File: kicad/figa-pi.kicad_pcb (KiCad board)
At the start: 4 copper layers, 65 x 56 mm, 147 parts, among them J1 BH-10(IDC-10MS), J2 PLS-2, J3 PBD-40(DS1023-2x20), J4 PLD-10(DS1021-2x5), J5 L829-1J1T-43, J6 POE connector, J7 PLS-1, J8 PLS-1, J9 PLS-1, U1 CAT24C32WI, U10 TLV62084DSGR, U11 TLV62084DSGR, U2 ASEMB-25.000MHZ-LC-T, U3 NUP4114UPXV6T1G, U5 10CL025ZE144, U6 KSZ9021GN, U7 CDCLVC1102PW, U9 TLV62084DSGR

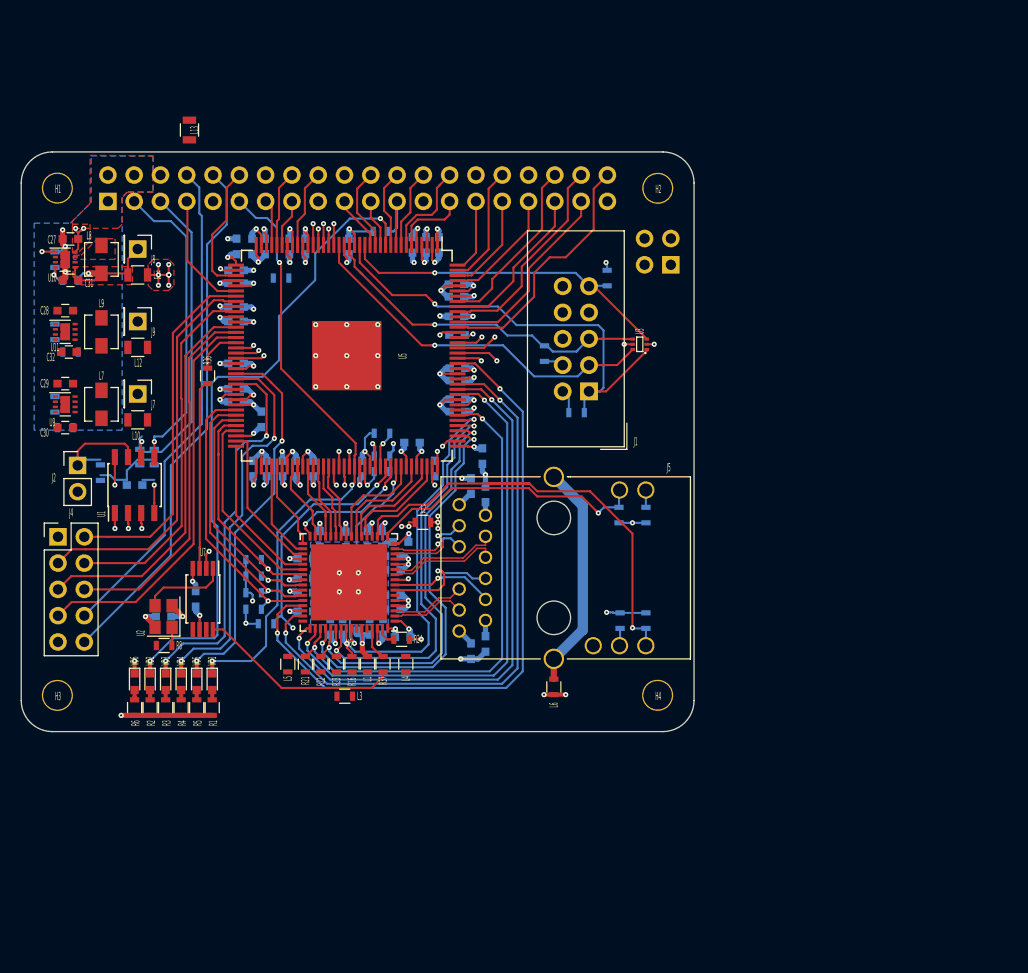
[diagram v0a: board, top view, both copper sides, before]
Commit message: Added LOGO as footprint Added fields for all components Renamed BOM file. Updated BOM file. Updated project fields.
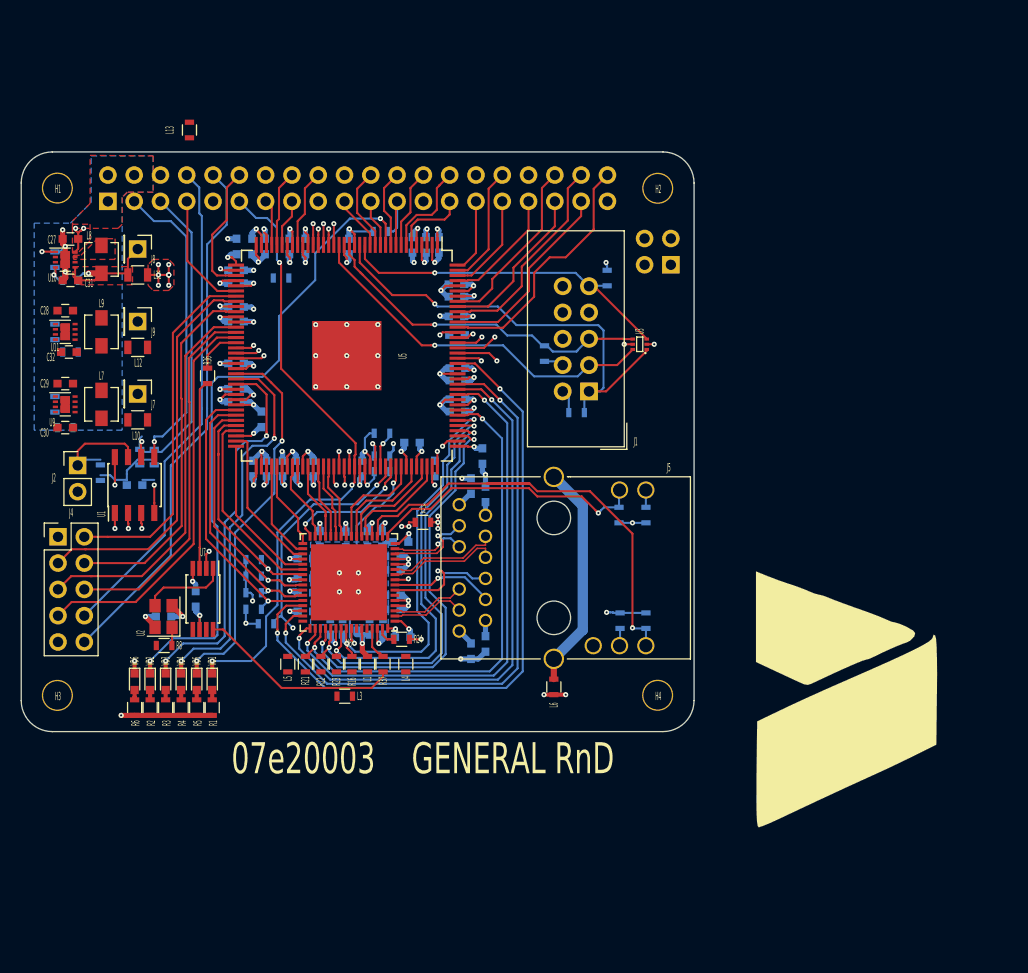
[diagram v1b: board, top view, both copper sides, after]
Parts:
- added G***: LOGO, library:LogoGenRND_18x25mm, F.Cu at (158.3, 113.7)
- C1, C10, C11, C12, C13, C18, C19, C2, C20, C21, C25, C3, C35, C36, C38, C39, C4, C41, C42, C43, C44, C45, C46, C47, C48, C5, C54, C56, C58, C60, C61, C63, C65, C66, C7, C8, C9: value 0.1u -> 0.1uF
- C14, C15, C16, C17: value 0.1u 16V -> 0.1uF
- C22, C23, C24, C26, C33, C34, C37, C40, C6, C62, C64: value 10u -> 10uF
- C27, C28, C29: value 10u 16V -> 10uF
- C30, C31, C32: value 22u 6v3 -> 22uF
- C49, C50, C51, C52, C53, C55, C57, C59: value 0.01u -> 0.01uF
- L13: footprint Inductors_SMD:L_0805 -> Inductors_SMD:L_0603
- R11, R12: value 3.9k -> 3.92k
- R30: value 178k 1% -> 127k 1%
- R31, R35: value 39.2k 1% -> 28k 1%
- R34: value 65.3k 1% -> 46.4k 1%
- U1: value CAT24C32WI -> 24LC32A/SN
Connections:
- net IO_85 renamed IO_31
- net IO_86 renamed IO_32
- net IO_87 renamed IO_28
- net IO_99 renamed IO_33
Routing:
- net (no net): track 0.00 -> 7.87 mm
- net +3V3: track 70.8 -> 64.1 mm
- net GND: track 221.8 -> 220.6 mm
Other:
- board text added: "07e20003"
- board text added: "GENERAL RnD"

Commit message: Removed footprint for unused components Updated 3d model for LQFP-144 Updated symbol library Updated schematics Updated PCB - finished routing
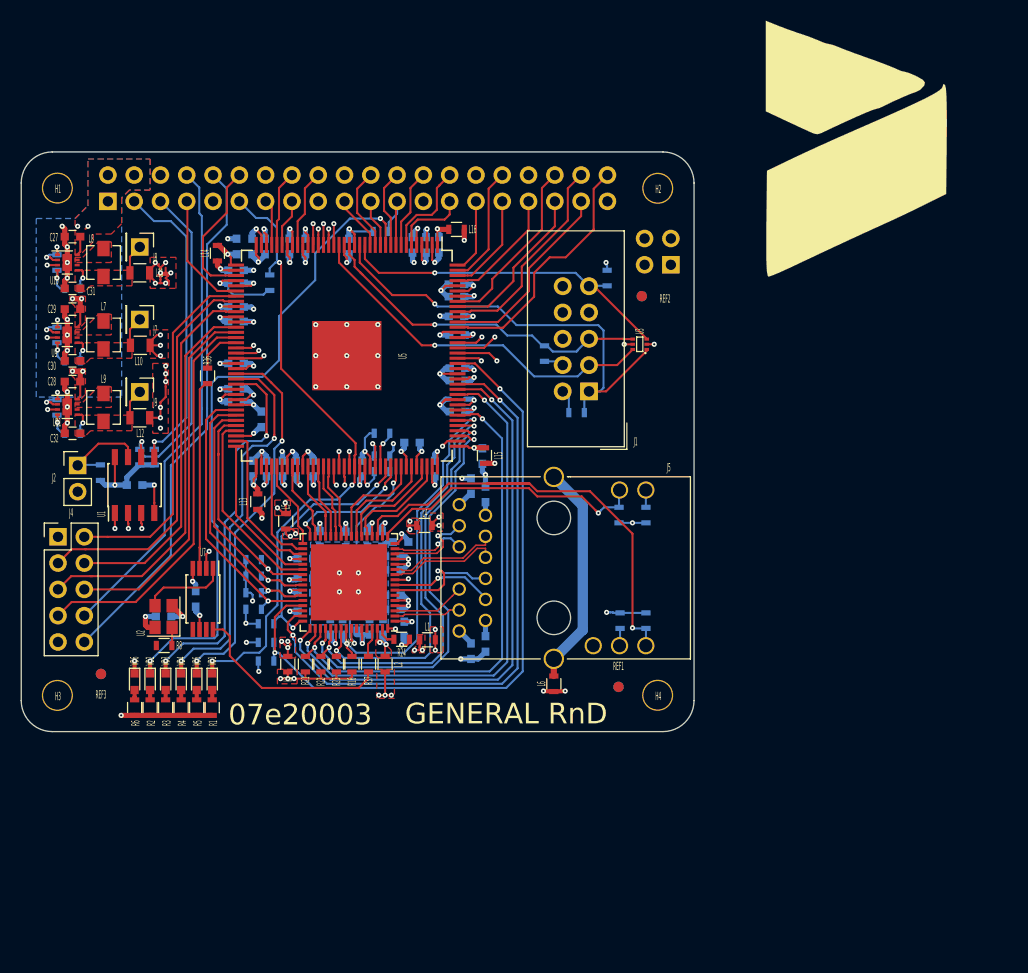
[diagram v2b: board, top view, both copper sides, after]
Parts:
- removed C51: 0.01uF, Capacitors_SMD:C_0603
- added L14: BLM18PG330SN1D, Inductors_SMD:L_0603, F.Cu at (97.5, 70.6)
- added L15: BLM18PG330SN1D, Inductors_SMD:L_0603, F.Cu at (123.3, 90.2)
- added L16: BLM18PG330SN1D, Inductors_SMD:L_0603, F.Cu at (120.6, 68.3)
- added R41: DNI_4.99k 1%, Resistors_SMD:R_0603, B.Cu at (102.2, 108.2)
- added R42: 1k, Resistors_SMD:R_0603, B.Cu at (102.2, 110.0)
- added REF1: Fiducial_1mm_Dia_2.54mm_Outer_CopperTop, Fiducials:Fiducial_1mm_Dia_2.54mm_Outer_CopperTop, F.Cu at (136.2, 112.5)
- added REF2: Fiducial_1mm_Dia_2.54mm_Outer_CopperTop, Fiducials:Fiducial_1mm_Dia_2.54mm_Outer_CopperTop, F.Cu at (138.5, 74.8)
- added REF3: Fiducial_1mm_Dia_2.54mm_Outer_CopperTop, Fiducials:Fiducial_1mm_Dia_2.54mm_Outer_CopperTop, B.Cu at (86.2, 111.2)
- added REF3: Fiducial_1mm_Dia_2.54mm_Outer_CopperTop, Fiducials:Fiducial_1mm_Dia_2.54mm_Outer_CopperTop, F.Cu at (86.2, 111.2)
- added REF4: Fiducial_1mm_Dia_2.54mm_Outer_CopperTop, Fiducials:Fiducial_1mm_Dia_2.54mm_Outer_CopperTop, B.Cu at (138.5, 74.8)
- added REF5: Fiducial_1mm_Dia_2.54mm_Outer_CopperTop, Fiducials:Fiducial_1mm_Dia_2.54mm_Outer_CopperTop, B.Cu at (136.2, 112.5)
- moved G*** 53.2 mm to (159.2, 60.5)
- moved L13 36.5 mm to (101.4, 94.6)
- moved C37 31.2 mm to (99.3, 70.0), turned to 90 degrees
- moved C49 28.1 mm to (101.0, 91.4), turned to 90 degrees
- moved C41 22.2 mm to (123.1, 90.2), turned to 270 degrees
- moved C45 19.6 mm to (118.9, 69.8), turned to 270 degrees
- moved L2 14.2 mm to (113.7, 110.3), turned to 270 degrees
- moved L5 13.8 mm to (104.1, 96.5), turned to 90 degrees
- moved L4 13.5 mm to (117.5, 96.9), turned to 0 degrees
- moved C32 7.86 mm to (83.5, 88.0)
- moved R34 7.85 mm to (83.5, 88.0)
- moved L9 7.30 mm to (86.5, 85.5)
- moved R35 7.30 mm to (82.0, 85.5)
- moved U11 7.25 mm to (83.0, 85.5)
- moved C29 7.23 mm to (83.5, 76.0)
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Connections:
- net 25M_A renamed /interface.sch/FPGA_25M
- net 25M_B renamed /ethernet.sch/PHY_25M
- net CLK_125M renamed /ethernet.sch/CLK_125M
- net DATA renamed /interface.sch/DATA
- net DCLK renamed /interface.sch/DCLK
- net GTX_CLK renamed /ethernet.sch/GTX_CLK
- net INT_N renamed /ethernet.sch/INT_N
- net IO_10 renamed /interface.sch/IO_10
- net IO_133 renamed /interface.sch/IO_133
- net IO_141 renamed /interface.sch/IO_141
- net IO_142 renamed /interface.sch/IO_142
- net IO_143 renamed /interface.sch/IO_143
- net IO_144 renamed /interface.sch/IO_144
- net IO_28 renamed /interface.sch/IO_28
- net IO_31 renamed /interface.sch/IO_31
- net IO_32 renamed /interface.sch/IO_32
- net IO_33 renamed /interface.sch/IO_33
- net IO_39 renamed /interface.sch/IO_39
- net IO_42 renamed /interface.sch/IO_42
- net IO_6 renamed /interface.sch/IO_6
- net IO_7 renamed /interface.sch/IO_7
- net IO_8 renamed /interface.sch/IO_8
- net JTAG_TCK renamed /interface.sch/JTAG_TCK
- net JTAG_TDI renamed /interface.sch/JTAG_TDI
- net JTAG_TDO renamed /interface.sch/JTAG_TDO
- net JTAG_TMS renamed /interface.sch/JTAG_TMS
- net PI_GPIO16/SPI1_CS0 renamed /interface.sch/PI_GPIO16/SPI1_CS0
- net PI_GPIO19/SPI1_MISO renamed /interface.sch/PI_GPIO19/SPI1_MISO
- net PI_GPIO20/SPI1_MOSI renamed /interface.sch/PI_GPIO20/SPI1_MOSI
- net PI_GPIO21/SPI1_SCLK renamed /interface.sch/PI_GPIO21/SPI1_SCLK
- net RX_CLK renamed /ethernet.sch/RX_CLK
- net SCL renamed /interface.sch/SCL
- net SDA renamed /interface.sch/SDA
- net TXD0 renamed /ethernet.sch/TXD0
- net TXD1 renamed /ethernet.sch/TXD1
- net TXD2 renamed /ethernet.sch/TXD2
- net TXD3 renamed /ethernet.sch/TXD3
- net TX_CLK renamed /ethernet.sch/TX_CLK
- net UART0_RX renamed /interface.sch/UART0_RX
- net UART0_TX renamed /interface.sch/UART0_TX
- net USER_LED0 renamed /ethernet.sch/USER_LED0
- net nCONFIG renamed /interface.sch/nCONFIG
- C11 pad 1: DVDDH -> /ethernet.sch/DVDDH
- C19 pad 1: DVDDH -> /ethernet.sch/DVDDH
- C23 pad 1: DVDDH -> /ethernet.sch/DVDDH
- C41 pad 1: Net-(C37-Pad1) -> Net-(C41-Pad1)
- C45 pad 1: Net-(C37-Pad1) -> Net-(C45-Pad1)
- C49 pad 1: Net-(C37-Pad1) -> Net-(C49-Pad1)
- C7 pad 1: DVDDH -> /ethernet.sch/DVDDH
- J3 pad 23: nSTATUS -> /interface.sch/nSTATUS
- L13 pad 2: Net-(C37-Pad1) -> Net-(C49-Pad1)
- L3 pad 1: DVDDH -> /ethernet.sch/DVDDH
- R15 pad 1: nSTATUS -> +3V3
- R15 pad 2: +3V3 -> /interface.sch/nSTATUS
- R17 pad 2: DVDDH -> +3V3
- R22 pad 2: DVDDH -> +3V3
- R23 pad 2: DVDDH -> +3V3
- R25 pad 1: DVDDH -> +3V3
- R26 pad 1: DVDDH -> +3V3
- R27 pad 1: DVDDH -> +3V3
- R28 pad 2: DVDDH -> +3V3
- R29 pad 1: DVDDH -> +3V3
- U5 pad 1: Net-(C37-Pad1) -> Net-(C45-Pad1)
- U5 pad 109: Net-(C37-Pad1) -> Net-(C41-Pad1)
- U5 pad 73: Net-(C37-Pad1) -> Net-(C49-Pad1)
- U5 pad 9: nSTATUS -> /interface.sch/nSTATUS
- U6 pad 18: DVDDH -> /ethernet.sch/DVDDH
- U6 pad 30: DVDDH -> /ethernet.sch/DVDDH
- U6 pad 40: DVDDH -> /ethernet.sch/DVDDH
- U6 pad 46: DVDDH -> /ethernet.sch/DVDDH
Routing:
- net +3V3: track 64.1 -> 108.0 mm, vias 29 -> 35
- net +2V5: track 10.0 -> 50.4 mm, vias 4 -> 7
- net GND: track 220.6 -> 245.3 mm, vias 78 -> 92
- net DVDDH: track 18.2 -> 0.00 mm, vias 7 -> 0
- net +1V2: track 35.6 -> 52.9 mm, vias 14 -> 28
- net /ethernet.sch/DVDDH: track 0.00 -> 11.0 mm, vias 0 -> 7
- net nSTATUS: track 7.76 -> 0.00 mm
- net (no net): track 7.87 -> 0.35 mm, vias 0 -> 3
- net /interface.sch/nSTATUS: track 0.00 -> 7.50 mm
- net +5V: track 4.52 -> 11.5 mm, vias 3 -> 7
- net /power.sch/3.3V_out: track 12.1 -> 5.24 mm
- net Net-(C37-Pad1): track 9.96 -> 3.85 mm, vias 4 -> 1
- net /power.sch/1.2V_out: track 0.00 -> 5.29 mm, vias 0 -> 1
- net /power.sch/2.5V_out: track 0.00 -> 5.24 mm, vias 0 -> 1
- net /ethernet.sch/DVDDL: track 11.0 -> 15.8 mm, vias 5 -> 7
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- added copper zone on F.Cu, net +1V2
- added copper zone on In2.Cu, net +1V2
- added copper zone on F.Cu, net +2V5
- added copper zone on In2.Cu, net +2V5
- added copper zone on In2.Cu, net +3V3
- added copper zone on In2.Cu, net +5V
- added copper zone on F.Cu, net /ethernet.sch/AVDDH
- added copper zone on In2.Cu, net /ethernet.sch/AVDDH
- added copper zone on F.Cu, net /ethernet.sch/AVDDL
- added copper zone on In2.Cu, net /ethernet.sch/AVDDL
- added copper zone on F.Cu, net /ethernet.sch/AVDDL_PLL
- added copper zone on In2.Cu, net /ethernet.sch/AVDDL_PLL
- added copper zone on F.Cu, net /ethernet.sch/DVDDH
- added copper zone on In2.Cu, net /ethernet.sch/DVDDH
- added copper zone on F.Cu, net /ethernet.sch/DVDDL
- added copper zone on In2.Cu, net /ethernet.sch/DVDDL
- added copper zone on F.Cu, net /power.sch/1.2V_out
- added copper zone on F.Cu, net /power.sch/2.5V_out
- added copper zone on F.Cu, net Net-(L7-Pad1)
- added copper zone on F.Cu, net Net-(L9-Pad1)

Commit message: add board name to pcb (figa-pi), move board number and correct company name
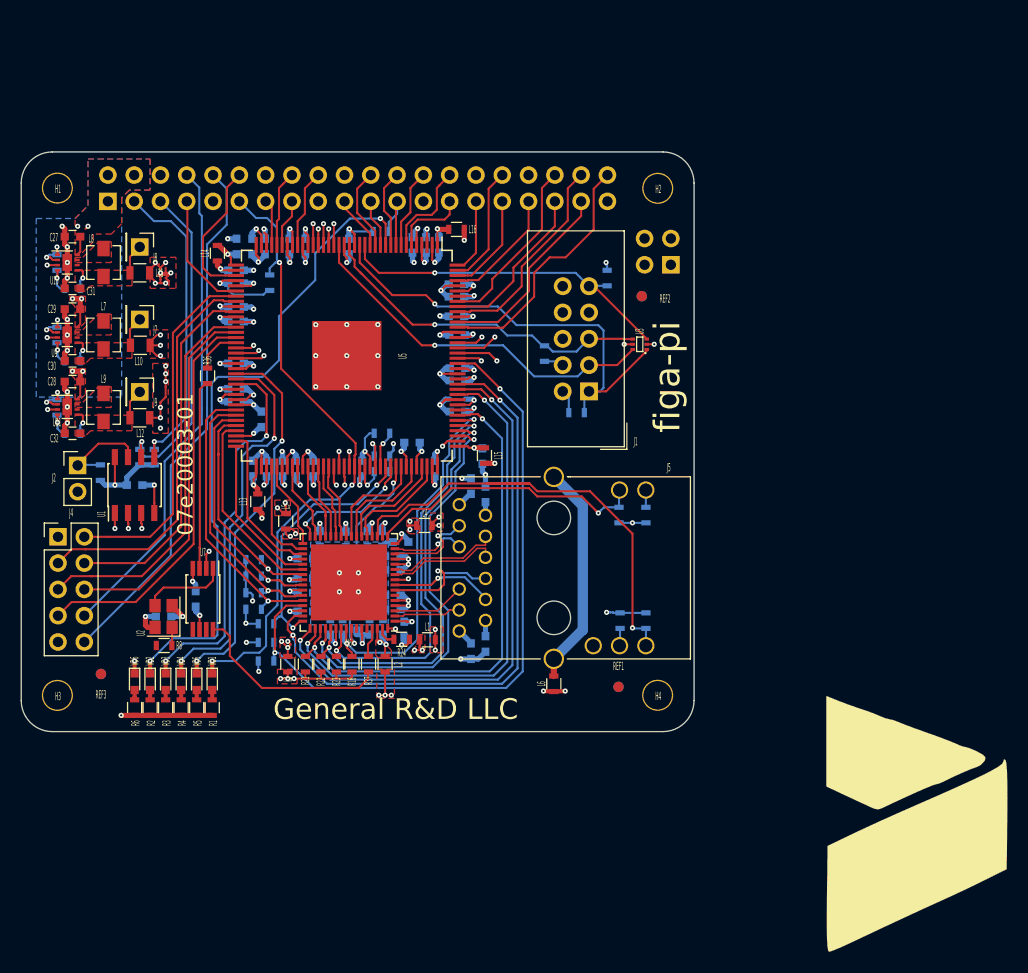
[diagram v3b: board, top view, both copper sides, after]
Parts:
- moved G*** 65.5 mm to (165.1, 125.7)
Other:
- board text added: "07e20003-01"
- board text added: "General R&D LLC"
- board text added: "figa-pi"
- board text removed: "07e20003"
- board text removed: "GENERAL RnD"
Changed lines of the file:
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@@
-(kicad_pcb (version 4) (host pcbnew 4.0.7)
+(kicad_pcb (version 4) (host pcbnew 4.0.6)
   (general
-    (links 0)
+    (links 482)
     (no_connects 0)
-    (area 69.386904 45.025 229.685714 119.158333)
+    (area 78.496355 60.76761 143.596357 116.867612)
     (thickness 1.6)
-    (drawings 56)
+    (drawings 57)
     (tracks 1841)
     (zones 0)
@@
   )
   (setup
-    (last_trace_width 0.15)
+    (last_trace_width 0.2)
     (user_trace_width 0.15)
     (user_trace_width 0.2)
@@
     (pad_to_paste_clearance -0.05)
     (aux_axis_origin 0 0)
+    (grid_origin 165.1 125.73)
     (visible_elements 7FFE7B7F)
     (pcbplotparams
@@
   )
   (module library:LogoGenRND_18x25mm (layer F.Cu)
-    (at 159.25 60.5)
+    (at 165.1 125.73)
     (fp_text reference G*** (at 0 0) (layer F.SilkS) hide
       (effects (font (thickness 0.3)))
@@
       (xy -7.249115 -2.893083) (xy -8.766371 -3.605225) (xy -8.766371 -12.356272) (xy -7.586283 -11.880815)) (layer F.SilkS) (width 0.01))
   )
-  (gr_text "GENERAL RnD" (at 125.4 115.1) (layer F.SilkS)
-    (effects (font (size 2 2) (thickness 0.3)))
+  (gr_text figa-pi (at 140.97 82.55 90) (layer F.SilkS)
+    (effects (font (size 2.5 2.5) (thickness 0.4)))
   )
-  (gr_text 07e20003 (at 105.5 115.2) (layer F.SilkS)
+  (gr_text "General R&D LLC" (at 114.72164 114.66576) (layer F.SilkS)
     (effects (font (size 2 2) (thickness 0.3)))
   )
+  (gr_text 07e20003-01 (at 94.4118 97.8789 90) (layer F.SilkS)
+    (effects (font (size 1.5 1.5) (thickness 0.3)) (justify left))
+  )
   (gr_text "If you want to use an SMT 40-pin header, please move the top edge up \nby 0.5mm and locate the header in the same location as the current TH part." (at 117.3 47.5) (layer Cmts.User)

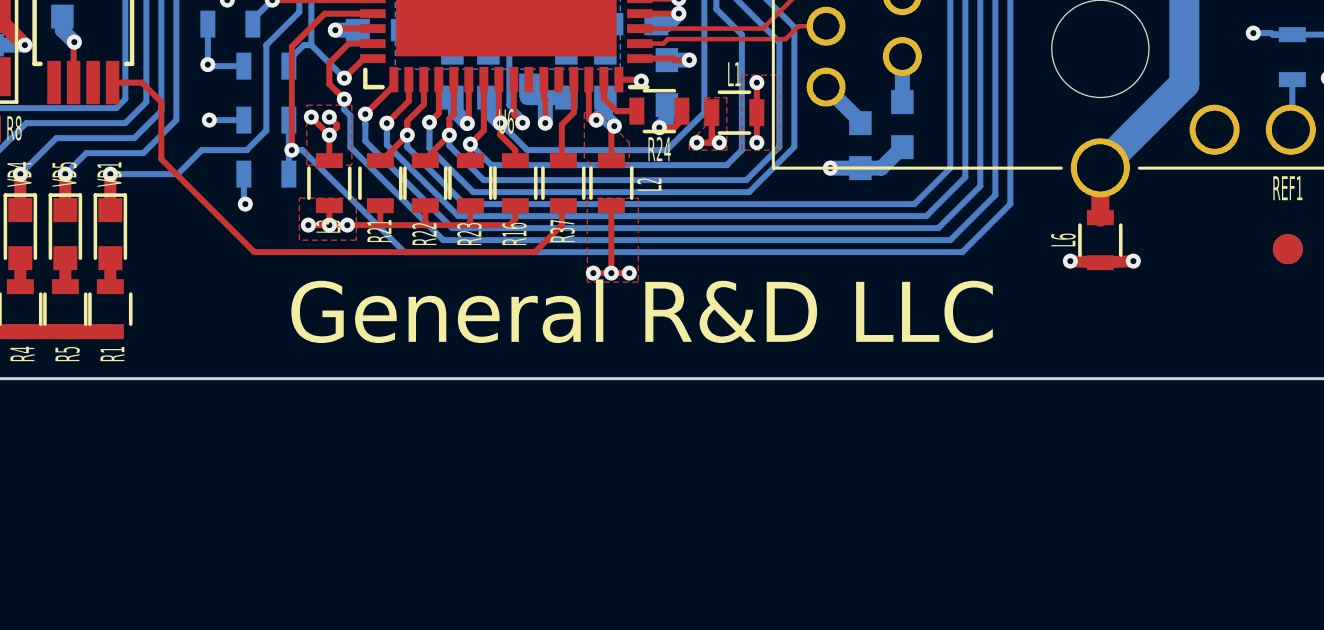
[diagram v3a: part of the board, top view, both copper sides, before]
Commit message: remove company name. url is more than enough
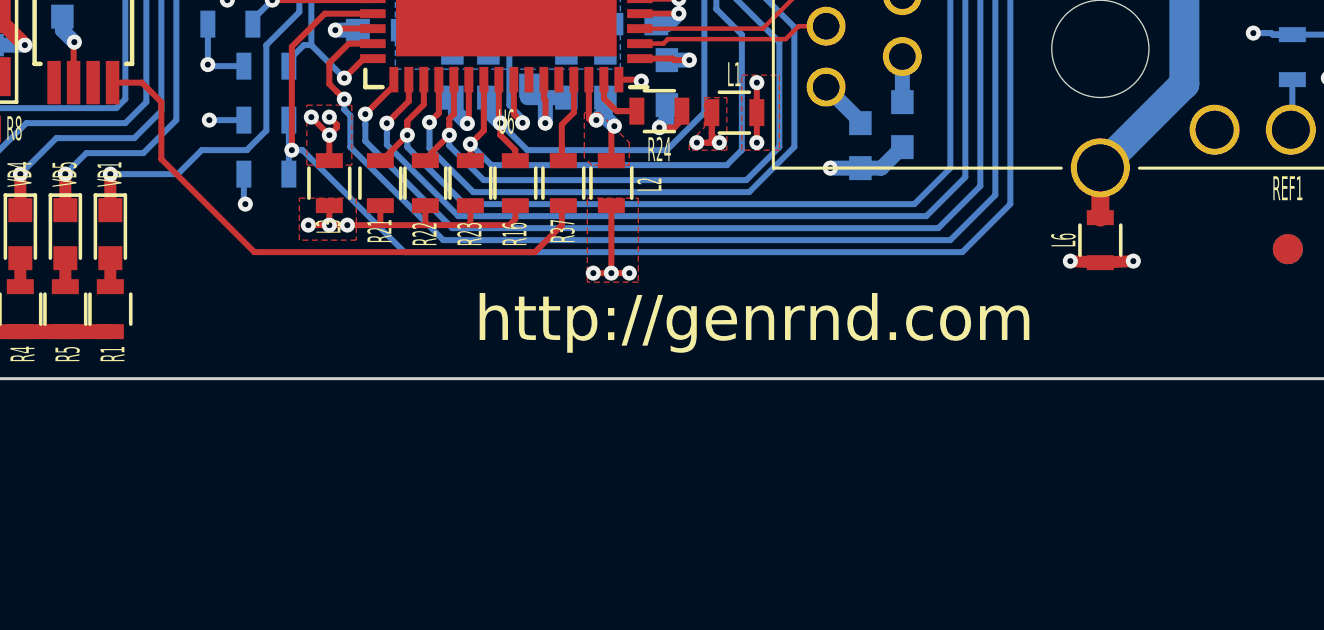
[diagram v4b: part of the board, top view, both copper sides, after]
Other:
- board text added: "http://genrnd.com"
- board text removed: "General R&D LLC"
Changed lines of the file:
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@@
       (xy -7.249115 -2.893083) (xy -8.766371 -3.605225) (xy -8.766371 -12.356272) (xy -7.586283 -11.880815)) (layer F.SilkS) (width 0.01))
+  )
+  (gr_text http://genrnd.com (at 118.4656 114.8334) (layer F.SilkS)
+    (effects (font (size 1.5 1.5) (thickness 0.3)))
   )
   (gr_text figa-pi (at 140.97 82.55 90) (layer F.SilkS)
     (effects (font (size 2.5 2.5) (thickness 0.4)))
   )
-  (gr_text "General R&D LLC" (at 114.72164 114.66576) (layer F.SilkS)
-    (effects (font (size 2 2) (thickness 0.3)))
-  )
   (gr_text 07e20003-01 (at 94.4118 97.8789 90) (layer F.SilkS)
